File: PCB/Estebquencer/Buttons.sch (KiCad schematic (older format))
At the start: 21 parts

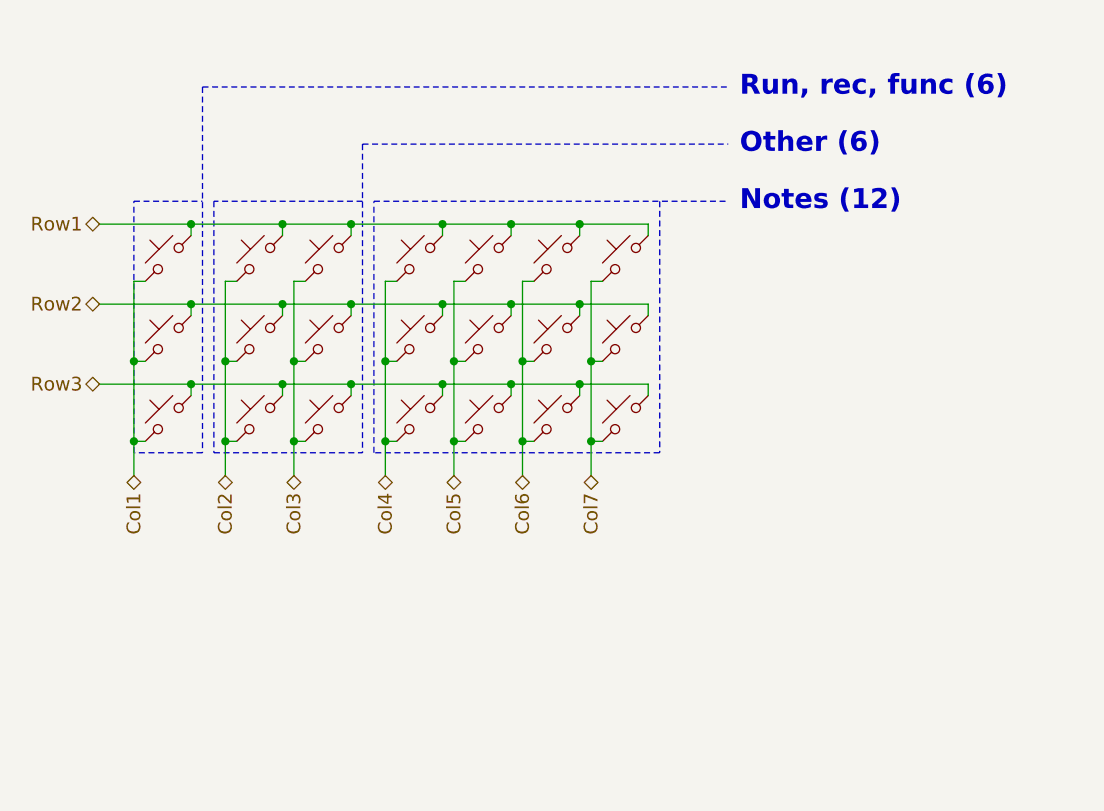
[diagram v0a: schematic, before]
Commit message: Se tuvo que cambiar el sistema de gestión de los LED y pulsadores. Con el charlieplexing no tenía los resultados esperados, así que se le añadió un HT16K33 para hacer las cosas más simples y fluídas. También se usará el mismo IC para la gestión de botones, ya que da opción.
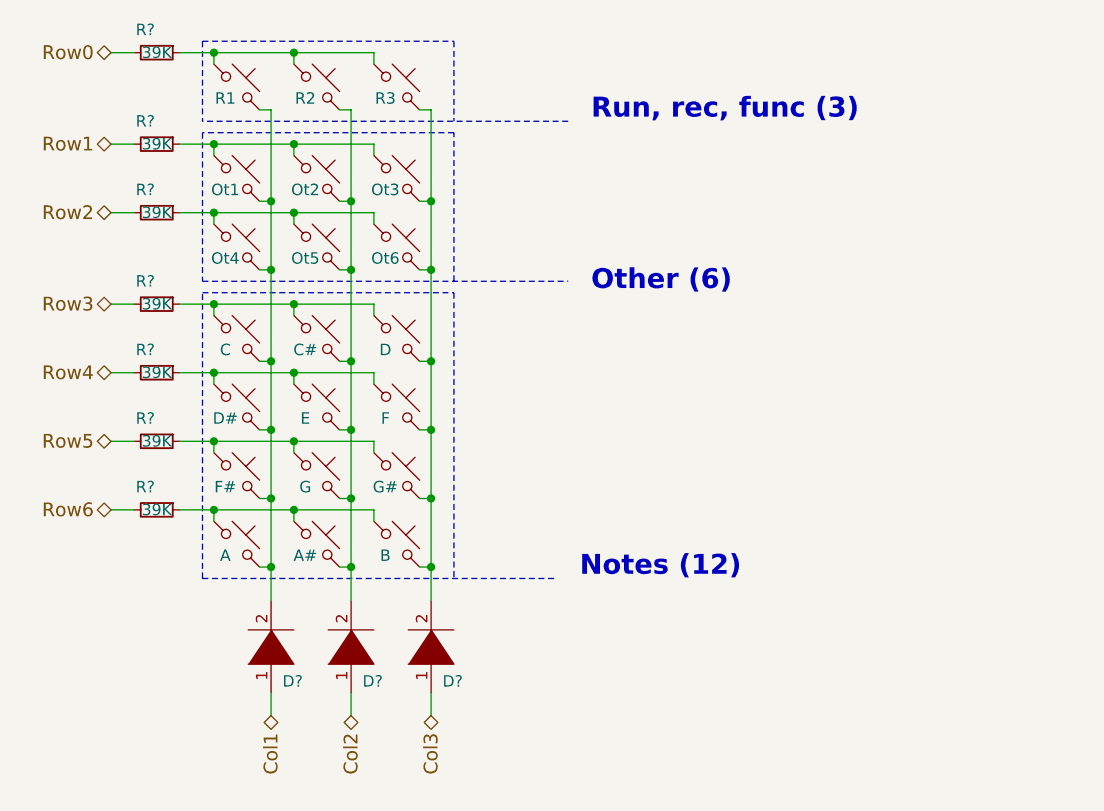
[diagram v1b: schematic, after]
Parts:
- added D? (x3): DIODE, symbol pspice:DIODE
- added R? (x7): 39K, symbol Device:R_Small
- SW?: value SW_Push_45deg -> Ot3
- SW?: value SW_Push_45deg -> Ot2
- SW?: value SW_Push_45deg -> Ot1
- SW?: value SW_Push_45deg -> Ot6
- SW?: value SW_Push_45deg -> Ot5
- SW?: value SW_Push_45deg -> Ot4
- SW?: value SW_Push_45deg -> R3
- SW?: value SW_Push_45deg -> R2
- SW?: value SW_Push_45deg -> R1
- SW?: value SW_Push_45deg -> D
- SW?: value SW_Push_45deg -> C#
- SW?: value SW_Push_45deg -> C
- SW?: value SW_Push_45deg -> F
- SW?: value SW_Push_45deg -> E
- SW?: value SW_Push_45deg -> D#
- SW?: value SW_Push_45deg -> G#
- SW?: value SW_Push_45deg -> G
- SW?: value SW_Push_45deg -> F#
- SW?: value SW_Push_45deg -> B
- SW?: value SW_Push_45deg -> A#
- SW?: value SW_Push_45deg -> A
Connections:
- net Col1: now also D?.1 (K); no longer SW?.2, SW?.2, SW?.2
- net Col2: now also D?.1 (K); no longer SW?.2, SW?.2, SW?.2
- net Col3: now also D?.1 (K); no longer SW?.2, SW?.2, SW?.2
- net Row1: now also R?.2; no longer SW?.1, SW?.1, SW?.1, SW?.1, SW?.1, SW?.1, SW?.1
- net Row2: now also R?.2; no longer SW?.1, SW?.1, SW?.1, SW?.1, SW?.1, SW?.1, SW?.1
- net Row3: now also R?.2; no longer SW?.1, SW?.1, SW?.1, SW?.1, SW?.1, SW?.1, SW?.1
- net Col4: no longer names the net of SW?.2, SW?.2, SW?.2
- net Col4: now also R?.1
- net Col5: no longer names the net of SW?.2, SW?.2, SW?.2
- net Col5: now also R?.1
- net Col6: no longer names the net of SW?.2, SW?.2, SW?.2
- net Col6: now also R?.1
- net Col7: no longer names the net of SW?.2, SW?.2, SW?.2
- net Col7: now also R?.1
- new net: D?.2 (A), SW?.1, SW?.1, SW?.1, SW?.1, SW?.1, SW?.1, SW?.1 (x3)
- new net: R?.1, SW?.2, SW?.2, SW?.2 (x3)
- new net Row0: R?.2
- new net Row4: R?.2
- new net Row5: R?.2
- new net Row6: R?.2
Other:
- note added: "Run, rec, func (3)"
- note removed: "Run, rec, func (6)"

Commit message: Había un pin desconectador de la matriz de LEDs
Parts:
- gave numbers to parts that had none: 31
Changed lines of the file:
@@
 $Descr A4 11693 8268
 encoding utf-8
-Sheet 10 11
+Sheet 6 11
 Title ""
 Date ""
@@
 $EndDescr
 $Comp
-L Switch:SW_Push_45deg SW?
+L Switch:SW_Push_45deg SW16
 U 1 1 5E68F4E0
 P 6300 2500
-F 0 "SW?" H 6300 2778 50  0001 C CNN
+F 0 "SW16" H 6300 2778 50  0001 C CNN
 F 1 "Ot3" V 6250 2450 50  0000 C CNN
 F 2 "" H 6300 2500 50  0001 C CNN
@@
 $EndComp
 $Comp
-L Switch:SW_Push_45deg SW?
+L Switch:SW_Push_45deg SW9
 U 1 1 5E68F7FF
 P 5950 2500
-F 0 "SW?" H 5950 2778 50  0001 C CNN
+F 0 "SW9" H 5950 2778 50  0001 C CNN
 F 1 "Ot2" V 5900 2450 50  0000 C CNN
 F 2 "" H 5950 2500 50  0001 C CNN
@@
 $EndComp
 $Comp
-L Switch:SW_Push_45deg SW?
+L Switch:SW_Push_45deg SW2
 U 1 1 5E68F80A
 P 5600 2500
-F 0 "SW?" H 5600 2778 50  0001 C CNN
+F 0 "SW2" H 5600 2778 50  0001 C CNN
 F 1 "Ot1" V 5550 2450 50  0000 C CNN
 F 2 "" H 5600 2500 50  0001 C CNN
@@
 $EndComp
 $Comp
-L Switch:SW_Push_45deg SW?
+L Switch:SW_Push_45deg SW17
 U 1 1 5E68FAA4
 P 6300 2800
-F 0 "SW?" H 6300 3078 50  0001 C CNN
+F 0 "SW17" H 6300 3078 50  0001 C CNN
 F 1 "Ot6" V 6250 2750 50  0000 C CNN
 F 2 "" H 6300 2800 50  0001 C CNN
@@
 $EndComp
 $Comp
-L Switch:SW_Push_45deg SW?
+L Switch:SW_Push_45deg SW10
 U 1 1 5E68FAAA
 P 5950 2800
-F 0 "SW?" H 5950 3078 50  0001 C CNN
+F 0 "SW10" H 5950 3078 50  0001 C CNN
 F 1 "Ot5" V 5900 2750 50  0000 C CNN
 F 2 "" H 5950 2800 50  0001 C CNN
@@
 $EndComp
 $Comp
-L Switch:SW_Push_45deg SW?
+L Switch:SW_Push_45deg SW3
 U 1 1 5E68FAB0
 P 5600 2800
-F 0 "SW?" H 5600 3078 50  0001 C CNN
+F 0 "SW3" H 5600 3078 50  0001 C CNN
 F 1 "Ot4" V 5550 2750 50  0000 C CNN
 F 2 "" H 5600 2800 50  0001 C CNN
@@
 $EndComp
 $Comp
-L Switch:SW_Push_45deg SW?
+L Switch:SW_Push_45deg SW8
 U 1 1 5E68FD69
 P 5950 2100
-F 0 "SW?" H 5950 2378 50  0001 C CNN
+F 0 "SW8" H 5950 2378 50  0001 C CNN
 F 1 "R2" V 5900 2050 50  0000 C CNN
 F 2 "" H 5950 2100 50  0001 C CNN
@@
 $EndComp
 $Comp
-L Switch:SW_Push_45deg SW?
+L Switch:SW_Push_45deg SW1
 U 1 1 5E68FD6F
 P 5600 2100
-F 0 "SW?" H 5600 2378 50  0001 C CNN
+F 0 "SW1" H 5600 2378 50  0001 C CNN
 F 1 "R1" V 5550 2050 50  0000 C CNN
 F 2 "" H 5600 2100 50  0001 C CNN
@@
 $EndComp
 $Comp
-L Switch:SW_Push_45deg SW?
+L Switch:SW_Push_45deg SW18
 U 1 1 5E68FD75
 P 6300 3200
-F 0 "SW?" H 6300 3478 50  0001 C CNN
+F 0 "SW18" H 6300 3478 50  0001 C CNN
 F 1 "D" V 6250 3150 50  0000 C CNN
 F 2 "" H 6300 3200 50  0001 C CNN
@@
 $EndComp
 $Comp
-L Switch:SW_Push_45deg SW?
+L Switch:SW_Push_45deg SW11
 U 1 1 5E68FD7B
 P 5950 3200
-F 0 "SW?" H 5950 3478 50  0001 C CNN
+F 0 "SW11" H 5950 3478 50  0001 C CNN
 F 1 "C#" V 5900 3150 50  0000 C CNN
 F 2 "" H 5950 3200 50  0001 C CNN
@@
 $EndComp
 $Comp
-L Switch:SW_Push_45deg SW?
+L Switch:SW_Push_45deg SW4
 U 1 1 5E68FD81
 P 5600 3200
-F 0 "SW?" H 5600 3478 50  0001 C CNN
+F 0 "SW4" H 5600 3478 50  0001 C CNN
 F 1 "C" V 5550 3150 50  0000 C CNN
 F 2 "" H 5600 3200 50  0001 C CNN
@@
 $EndComp
 $Comp
-L Switch:SW_Push_45deg SW?
+L Switch:SW_Push_45deg SW19
 U 1 1 5E68FD87
 P 6300 3500
-F 0 "SW?" H 6300 3778 50  0001 C CNN
+F 0 "SW19" H 6300 3778 50  0001 C CNN
 F 1 "F" V 6250 3450 50  0000 C CNN
 F 2 "" H 6300 3500 50  0001 C CNN
@@
 $EndComp
 $Comp
-L Switch:SW_Push_45deg SW?
+L Switch:SW_Push_45deg SW12
 U 1 1 5E68FD8D
 P 5950 3500
-F 0 "SW?" H 5950 3778 50  0001 C CNN
+F 0 "SW12" H 5950 3778 50  0001 C CNN
 F 1 "E" V 5900 3450 50  0000 C CNN
 F 2 "" H 5950 3500 50  0001 C CNN
@@
 $EndComp
 $Comp
-L Switch:SW_Push_45deg SW?
+L Switch:SW_Push_45deg SW5
 U 1 1 5E68FD93
 P 5600 3500
-F 0 "SW?" H 5600 3778 50  0001 C CNN
+F 0 "SW5" H 5600 3778 50  0001 C CNN
 F 1 "D#" V 5550 3450 50  0000 C CNN
 F 2 "" H 5600 3500 50  0001 C CNN
@@
 $EndComp
 $Comp
-L Switch:SW_Push_45deg SW?
+L Switch:SW_Push_45deg SW20
 U 1 1 5E6900AF
 P 6300 3800
-F 0 "SW?" H 6300 4078 50  0001 C CNN
+F 0 "SW20" H 6300 4078 50  0001 C CNN
 F 1 "G#" V 6250 3750 50  0000 C CNN
 F 2 "" H 6300 3800 50  0001 C CNN
@@
 $EndComp
 $Comp
-L Switch:SW_Push_45deg SW?
+L Switch:SW_Push_45deg SW13
 U 1 1 5E6900B5
 P 5950 3800
-F 0 "SW?" H 5950 4078 50  0001 C CNN
+F 0 "SW13" H 5950 4078 50  0001 C CNN
 F 1 "G" V 5900 3750 50  0000 C CNN
 F 2 "" H 5950 3800 50  0001 C CNN
@@
 $EndComp
 $Comp
-L Switch:SW_Push_45deg SW?
+L Switch:SW_Push_45deg SW6
 U 1 1 5E6900BB
 P 5600 3800
-F 0 "SW?" H 5600 4078 50  0001 C CNN
+F 0 "SW6" H 5600 4078 50  0001 C CNN
 F 1 "F#" V 5550 3750 50  0000 C CNN
 F 2 "" H 5600 3800 50  0001 C CNN
@@
 $EndComp
 $Comp
-L Switch:SW_Push_45deg SW?
+L Switch:SW_Push_45deg SW21
 U 1 1 5E6900C1
 P 6300 4100
-F 0 "SW?" H 6300 4378 50  0001 C CNN
+F 0 "SW21" H 6300 4378 50  0001 C CNN
 F 1 "B" V 6250 4050 50  0000 C CNN
 F 2 "" H 6300 4100 50  0001 C CNN
@@
 $EndComp
 $Comp
-L Switch:SW_Push_45deg SW?
+L Switch:SW_Push_45deg SW14
 U 1 1 5E6900C7
 P 5950 4100
-F 0 "SW?" H 5950 4378 50  0001 C CNN
+F 0 "SW14" H 5950 4378 50  0001 C CNN
 F 1 "A#" V 5900 4050 50  0000 C CNN
 F 2 "" H 5950 4100 50  0001 C CNN
@@
 $EndComp
 $Comp
-L Switch:SW_Push_45deg SW?
+L Switch:SW_Push_45deg SW7
 U 1 1 5E6900CD
 P 5600 4100
-F 0 "SW?" H 5600 4378 50  0001 C CNN
+F 0 "SW7" H 5600 4378 50  0001 C CNN
 F 1 "A" V 5550 4050 50  0000 C CNN
 F 2 "" H 5600 4100 50  0001 C CNN
@@
 Row0
 $Comp
-L Switch:SW_Push_45deg SW?
+L Switch:SW_Push_45deg SW15
 U 1 1 5E68FD63
 P 6300 2100
-F 0 "SW?" H 6300 2378 50  0001 C CNN
+F 0 "SW15" H 6300 2378 50  0001 C CNN
 F 1 "R3" V 6250 2050 50  0000 C CNN
 F 2 "" H 6300 2100 50  0001 C CNN
@@
 Row6
 $Comp
-L Device:R_Small R?
+L Device:R_Small R8
 U 1 1 5EA311E3
 P 5250 1950
-F 0 "R?" V 5150 1900 50  0000 C CNN
+F 0 "R8" V 5150 1900 50  0000 C CNN
 F 1 "39K" V 5250 1950 50  0000 C CNN
 F 2 "" H 5250 1950 50  0001 C CNN
@@
 $EndComp
 $Comp
-L Device:R_Small R?
+L Device:R_Small R9
 U 1 1 5EA31252
 P 5250 2350
-F 0 "R?" V 5150 2300 50  0000 C CNN
+F 0 "R9" V 5150 2300 50  0000 C CNN
 F 1 "39K" V 5250 2350 50  0000 C CNN
 F 2 "" H 5250 2350 50  0001 C CNN
@@
 $EndComp
 $Comp
-L Device:R_Small R?
+L Device:R_Small R10
 U 1 1 5EA312D0
 P 5250 2650
-F 0 "R?" V 5150 2600 50  0000 C CNN
+F 0 "R10" V 5150 2600 50  0000 C CNN
 F 1 "39K" V 5250 2650 50  0000 C CNN
 F 2 "" H 5250 2650 50  0001 C CNN
@@
 $EndComp
 $Comp
-L Device:R_Small R?
+L Device:R_Small R11
 U 1 1 5EA312D6
 P 5250 3050
-F 0 "R?" V 5150 3000 50  0000 C CNN
+F 0 "R11" V 5150 3000 50  0000 C CNN
 F 1 "39K" V 5250 3050 50  0000 C CNN
 F 2 "" H 5250 3050 50  0001 C CNN
@@
 $EndComp
 $Comp
-L Device:R_Small R?
+L Device:R_Small R12
 U 1 1 5EA332EC
 P 5250 3350
-F 0 "R?" V 5150 3300 50  0000 C CNN
+F 0 "R12" V 5150 3300 50  0000 C CNN
 F 1 "39K" V 5250 3350 50  0000 C CNN
 F 2 "" H 5250 3350 50  0001 C CNN
@@
 $EndComp
 $Comp
-L Device:R_Small R?
+L Device:R_Small R13
 U 1 1 5EA332F2
 P 5250 3650
-F 0 "R?" V 5150 3600 50  0000 C CNN
+F 0 "R13" V 5150 3600 50  0000 C CNN
 F 1 "39K" V 5250 3650 50  0000 C CNN
 F 2 "" H 5250 3650 50  0001 C CNN
@@
 $EndComp
 $Comp
-L Device:R_Small R?
+L Device:R_Small R14
 U 1 1 5EA35284
 P 5250 3950
-F 0 "R?" V 5150 3900 50  0000 C CNN
+F 0 "R14" V 5150 3900 50  0000 C CNN
 F 1 "39K" V 5250 3950 50  0000 C CNN
 F 2 "" H 5250 3950 50  0001 C CNN
@@
 	5150 3950 5050 3950
 $Comp
-L pspice:DIODE D?
+L pspice:DIODE D38
 U 1 1 5EA5C64C
 P 5750 4550
-F 0 "D?" V 5600 4500 50  0000 R CNN
+F 0 "D38" V 5600 4500 50  0000 R CNN
 F 1 "DIODE" V 5705 4422 50  0001 R CNN
 F 2 "" H 5750 4550 50  0001 C CNN
@@
 $EndComp
 $Comp
-L pspice:DIODE D?
+L pspice:DIODE D39
 U 1 1 5EA5C73E
 P 6100 4550
-F 0 "D?" V 5950 4500 50  0000 R CNN
+F 0 "D39" V 5950 4500 50  0000 R CNN
 F 1 "DIODE" V 6055 4422 50  0001 R CNN
 F 2 "" H 6100 4550 50  0001 C CNN
@@
 $EndComp
 $Comp
-L pspice:DIODE D?
+L pspice:DIODE D40
 U 1 1 5EA5C80E
 P 6450 4550
-F 0 "D?" V 6300 4500 50  0000 R CNN
+F 0 "D40" V 6300 4500 50  0000 R CNN
 F 1 "DIODE" V 6405 4422 50  0001 R CNN
 F 2 "" H 6450 4550 50  0001 C CNN
